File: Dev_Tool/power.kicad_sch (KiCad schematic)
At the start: 53 parts, among them SW1 SW_Push, U1 USB2514B-AEZC, U10 EPM7032SLC44-10, U11 SN74HCT245DWR, U12 SN74LVC1G07DBV, U13 SN74LVC1G07DBV, U14 SN74LVC1G07DBV, U15 SN74LVC1G07DBV, U16 SN74LVC1G07DBV, U17 SN74LVC1G07DBV, U18 SN74LVC1G07DBV, U19 SN74LVC1G07DBV, U20 SN74LVC1G07DBV, U21 SN74LVC1G07DBV, U22 SN74LVC1G07DBV, U23 LM1117-3.3, U24 APX803-31SAG-7, U25 SN74LVC1G07DBV, U4 MCP2221A-I/ST, U5 PCA9535PW, U6 MCP2200-I/SS, U7 MAX3243ECDB, U8 MCP2200-I/SS, U9 MAX3243ECDB

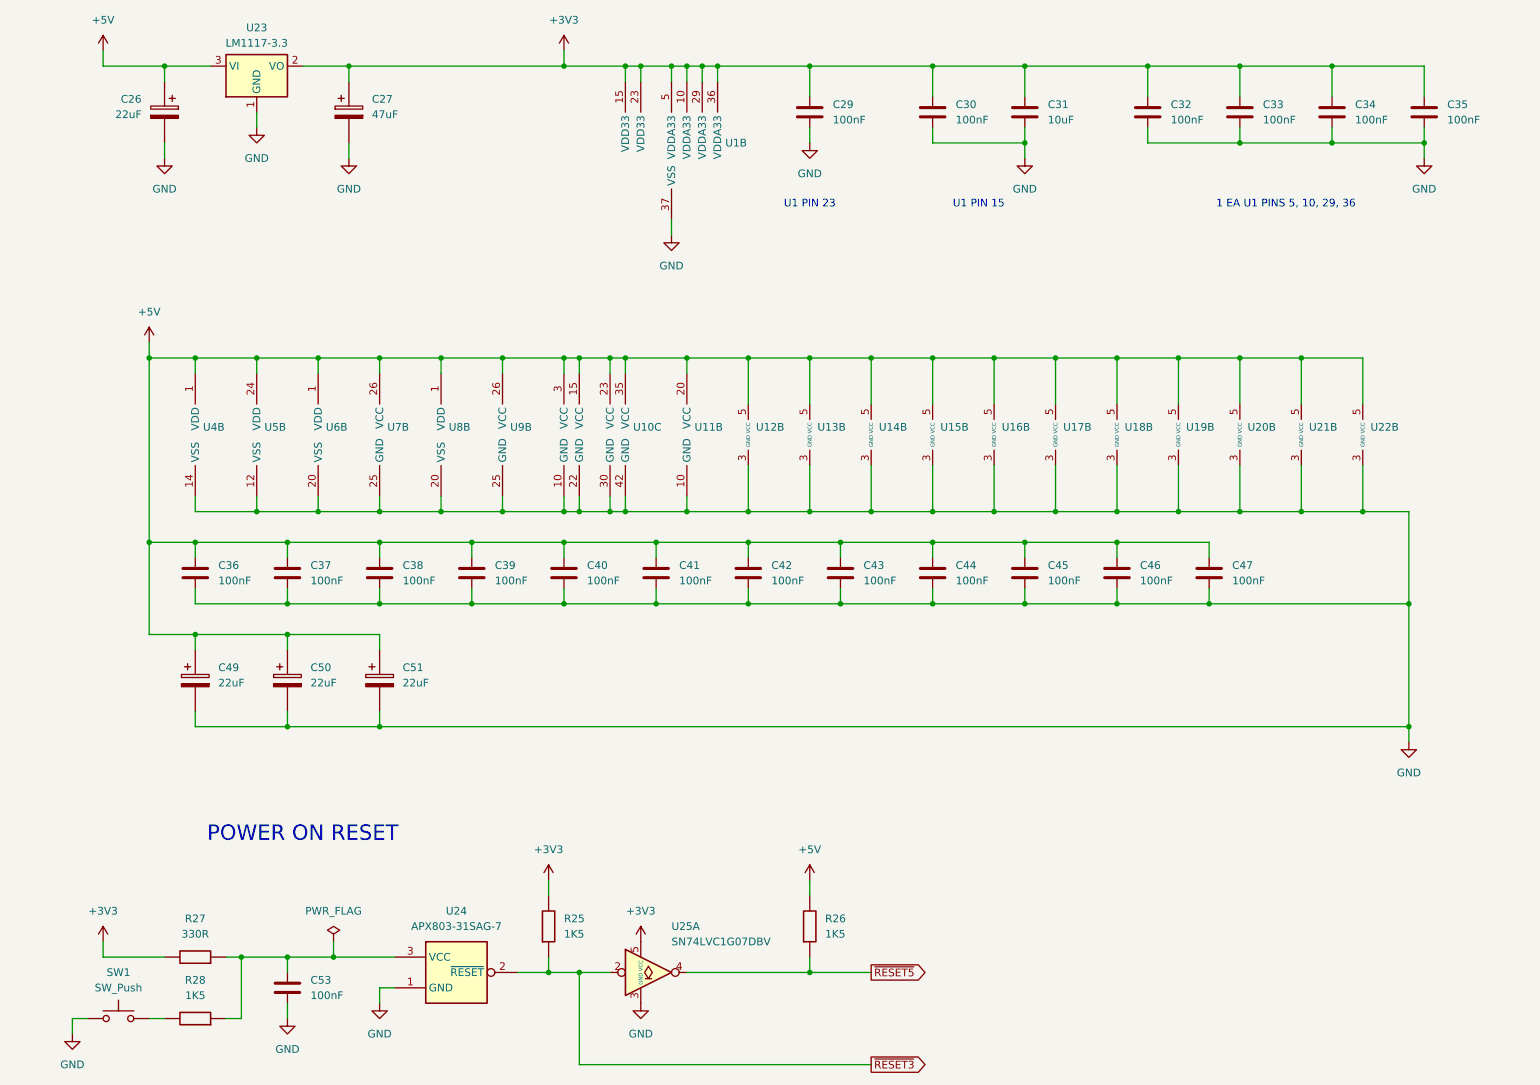
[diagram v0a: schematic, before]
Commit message: Change to FTDI FT232RN USB-serial converter
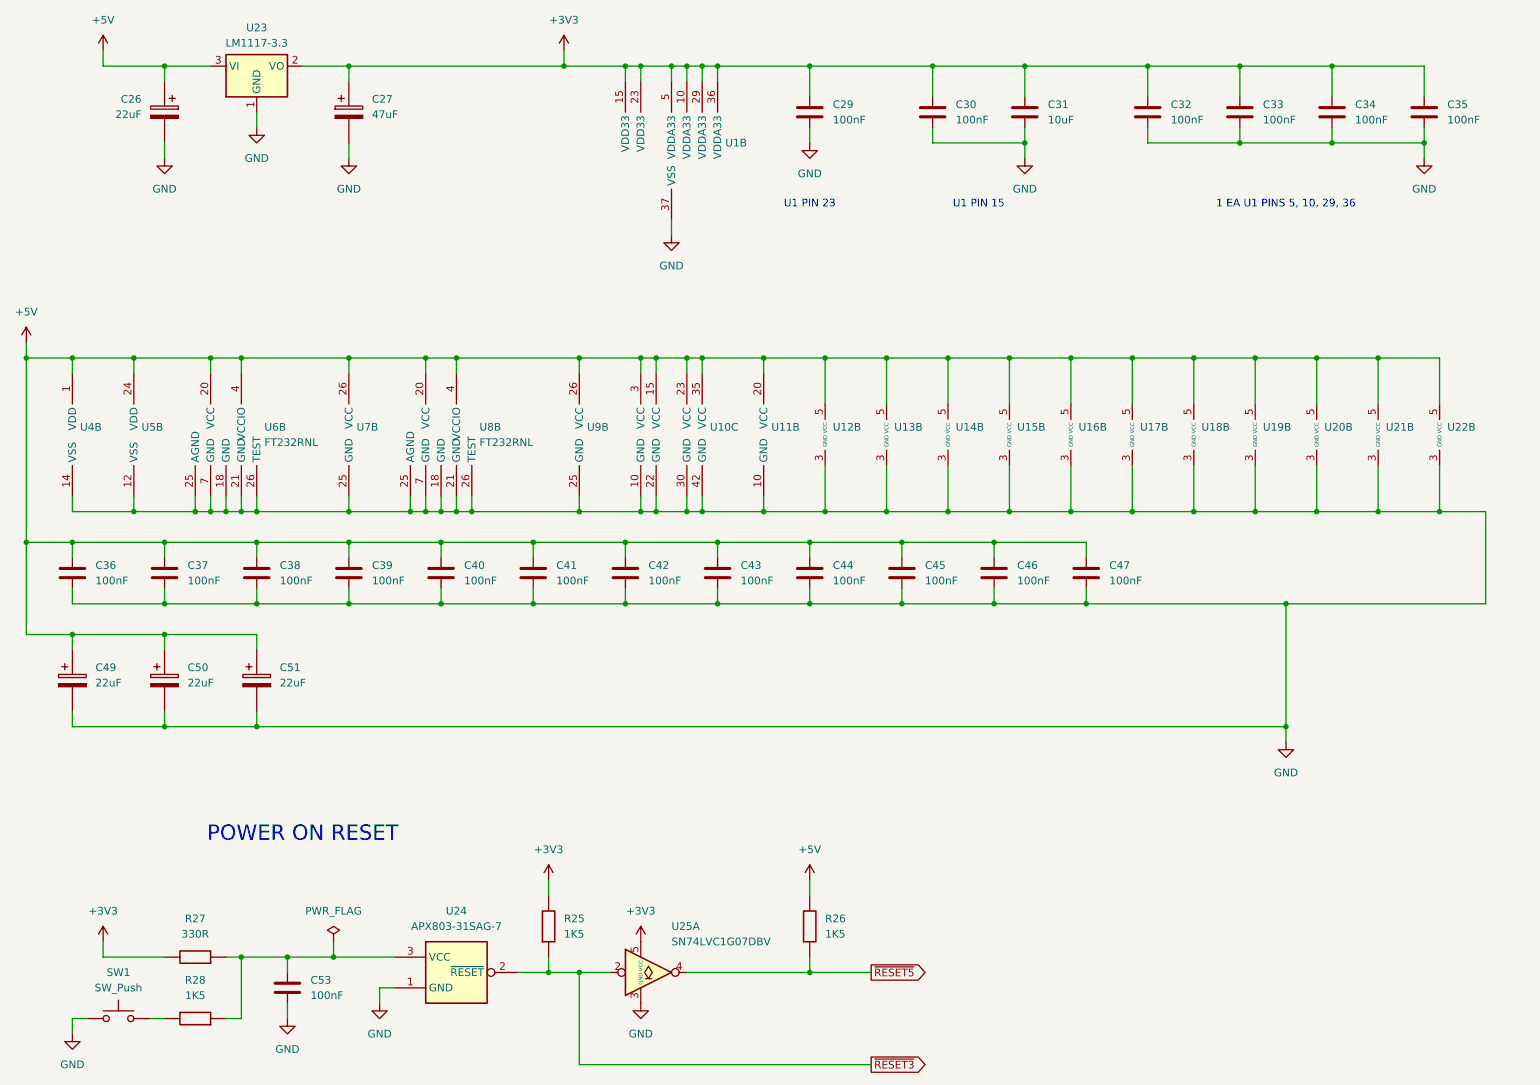
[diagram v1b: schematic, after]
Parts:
- removed U6, U8: MCP2200-I/SS, COMET_footprints:Package_SSOP-20_5.3x7.2mm_P0.65, symbol Dev_Tool:MCP2200-I/SS
- added U6, U8: FT232RNL, COMET_footprints:Package_SSOP-28_5.3x10.2mm_P0.65mm, symbol Dev_Tool:FT232RNL
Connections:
- net +5V: now also U6.20 (VCC), U6.4 (VCCIO), U8.20 (VCC), U8.4 (VCCIO)
- net GND: now also U6.18 (GND), U6.21 (GND), U6.25 (AGND), U6.26 (TEST), U6.7 (GND), U8.18 (GND), U8.21 (GND), U8.25 (AGND), U8.26 (TEST), U8.7 (GND)
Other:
- moved on the sheet: C36, C37, C38, C39, C40, C41, C42, C43, C44, C45, C46, C47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

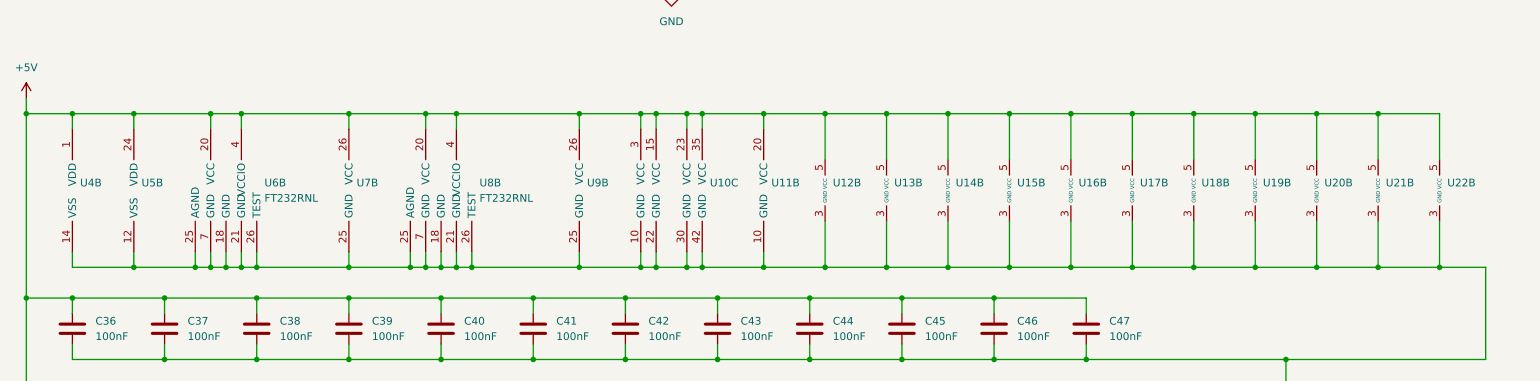
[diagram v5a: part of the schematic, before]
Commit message: Add reset for 5V devices when hub is suspended
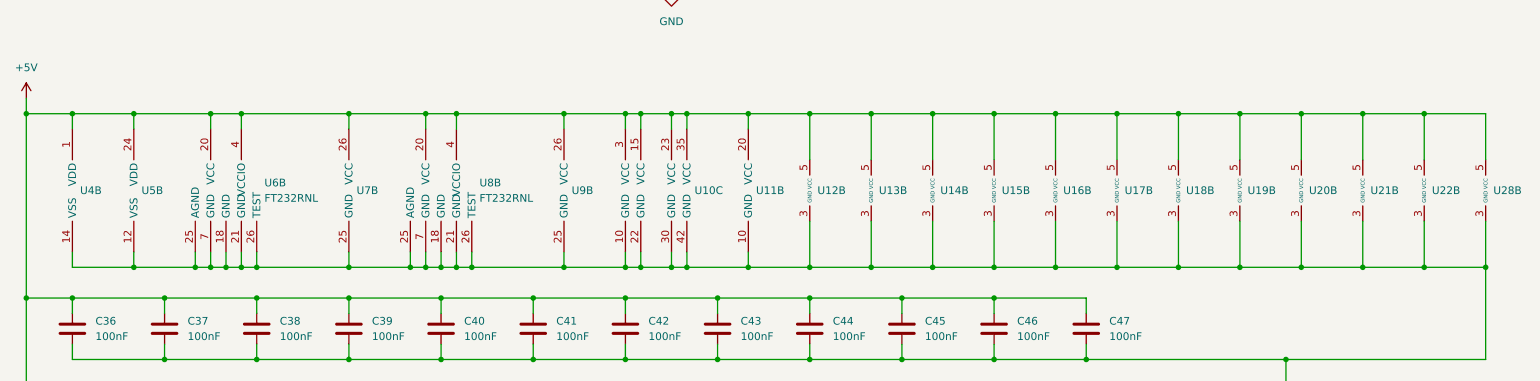
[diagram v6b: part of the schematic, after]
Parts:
- added U28: SN74LVC1G07DBV, COMET_footprints:Package_SOT23-5, symbol COMET_symbols:74x1G07
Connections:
- net +5V: now also U28.5 (VCC)
- net GND: now also U28.3 (GND)
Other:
- moved on the sheet: U10C, U11B, U12B, U13B, U14B, U15B, U16B, U17B, U18B, U19B, U20B, U21B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
